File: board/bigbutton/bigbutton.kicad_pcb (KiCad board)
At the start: 2 copper layers, 58 x 64 mm, 57 parts, among them J1 SWD, J2 USB_C_Receptacle_USB2.0, SW1 RESET, SW2 SMOL, SW3 LORGE, SW4 BOOT0, U1 STM32F303CBTx, U2 ATECC608A-SSHDA, U3 USBLC6-2, U4 SN74LV1T34DBV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

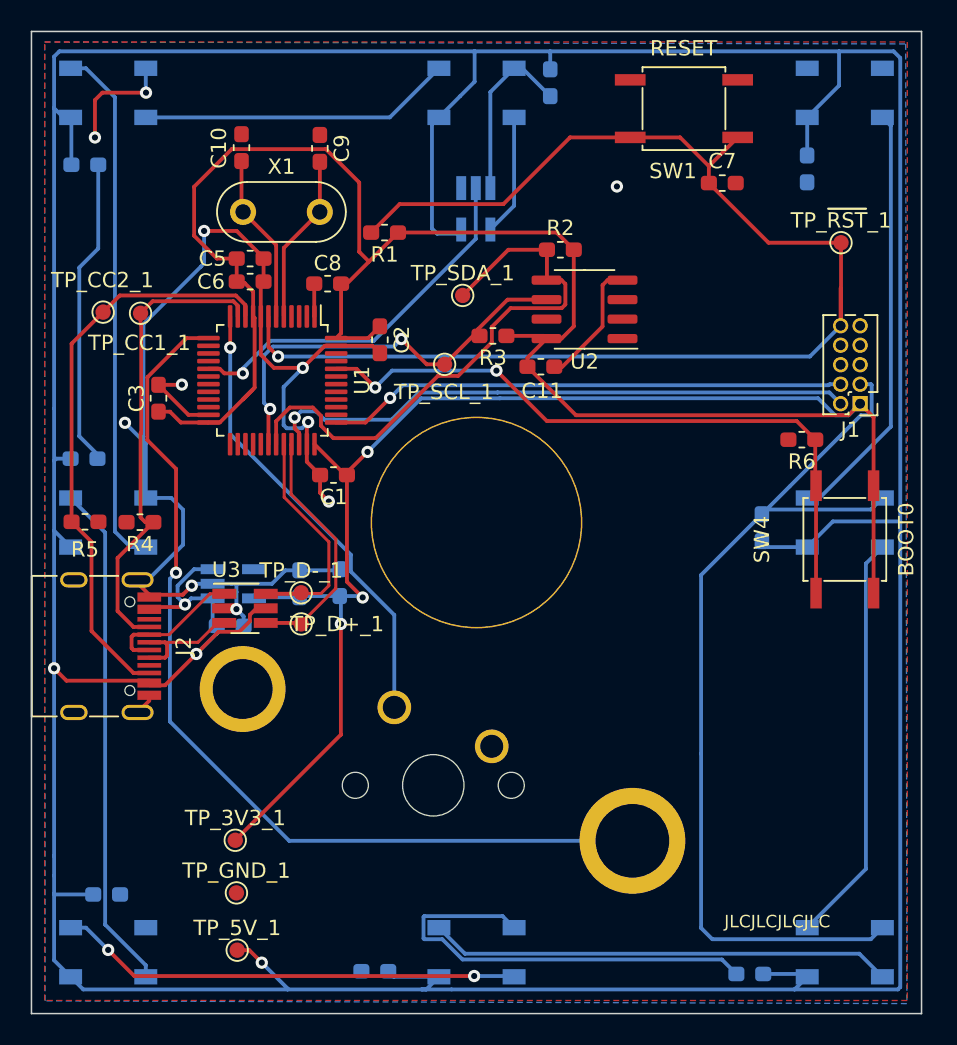
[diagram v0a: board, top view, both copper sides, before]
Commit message: Adjust board, add trans symbol to silkscreen
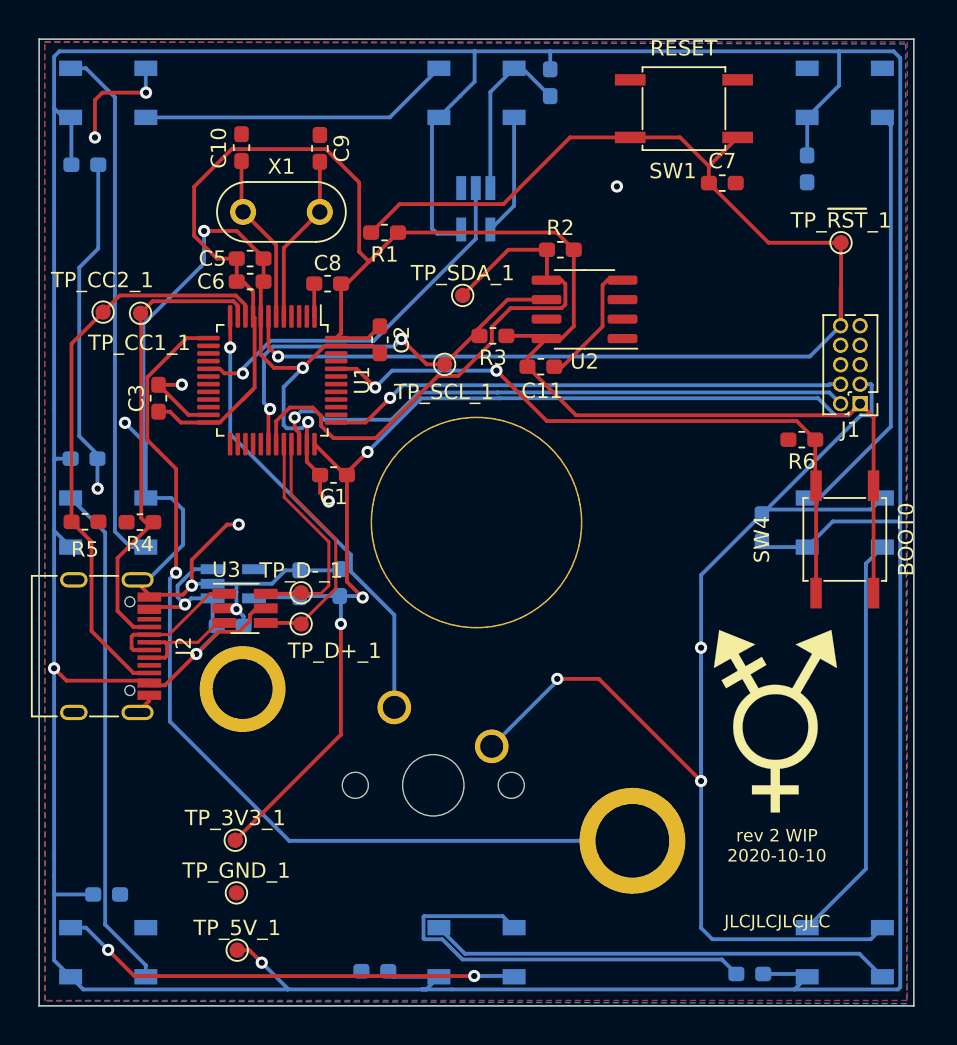
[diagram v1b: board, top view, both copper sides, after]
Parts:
- added G0: LOGO, bigbutton:trans, F.Cu at (124.2, 117.6)
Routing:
- net GND: track 229.5 -> 264.2 mm, vias 11 -> 16
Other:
- board size 58 x 64 mm -> 57 x 63 mm
- board text added: "rev 2 WIP 2020-10-10"

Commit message: Update footprint for bigbutton
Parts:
- X1: footprint Crystal:Resonator-2Pin_W8.0mm_H3.5mm -> Crystal:Resonator-2Pin_W10.0mm_H5.0mm
- moved C9 2.02 mm to (94.8, 78.6)
- moved C10 1.97 mm to (89.8, 78.6)
- moved R1 1.34 mm to (100.0, 85.2), turned to 90 degrees
- moved X1 1.06 mm to (89.8, 83.7)
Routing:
- net +3V3: track 188.3 -> 183.9 mm, vias 3 -> 5
- net /~RST: track 87.6 -> 84.9 mm
- net Net-(C9-Pad2): track 11.0 -> 13.1 mm
- net Net-(C10-Pad2): track 11.2 -> 13.0 mm
- net Net-(SW2-Pad1): track 29.9 -> 30.5 mm
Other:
- board text added: "rev 2 WIP 2020-10-18"
- board text removed: "rev 2 WIP 2020-10-10"

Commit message: Hopefully revision 2
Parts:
- C1, C10, C11, C12, C13, C14, C15, C16, C17, C18, C19, C2, C20, C21, C3, C4, C5, C6, C7, C8, C9: footprint Capacitor_SMD:C_0603_1608Metric_Pad1.05x0.95mm_HandSolder -> Capacitor_SMD:C_0603_1608Metric
- R1, R2, R3, R4, R5, R6: footprint Resistor_SMD:R_0603_1608Metric_Pad1.05x0.95mm_HandSolder -> Resistor_SMD:R_0603_1608Metric
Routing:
- net +3V3: track 183.9 -> 156.6 mm
- net +5V: track 317.3 -> 320.2 mm
- net GND: track 264.2 -> 265.4 mm
- net Net-(D4-Pad2): track 30.2 -> 30.9 mm
- net Net-(SW2-Pad1): track 30.5 -> 29.9 mm
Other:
- net class Default removed

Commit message: Add gerbers
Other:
- board text added: "bigbutton rev 2 2021-04-24"
- board text removed: "rev 2 WIP 2020-10-18"
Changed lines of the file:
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@@
   (gr_line (start 76.5 73.5) (end 133.5 73.5) (layer "Edge.Cuts") (width 0.1))
   (gr_line (start 76.5 136.5) (end 76.5 73.5) (layer "Edge.Cuts") (width 0.1))
-  (gr_text "rev 2 WIP\n2020-10-18" (at 124.5746 126.0602) (layer "F.SilkS")
+  (gr_text "bigbutton rev 2\n2021-04-24" (at 124.5746 126.0602) (layer "F.SilkS")
     (effects (font (size 0.8128 0.8128) (thickness 0.1524)))
   )
